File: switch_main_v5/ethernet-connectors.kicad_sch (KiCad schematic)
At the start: 9 parts, among them J2401 JST-GH-2-Horizontal, J2402 JST-GH-2-Horizontal, J2403 MSPE-J2L0-B00, J2404 MSPE-J2L0-B00, J2405 MSPE-J2L0-x00, J2406 MSPE-J2L0-x00, J2407 ARJM11D7-502-AB-EW2

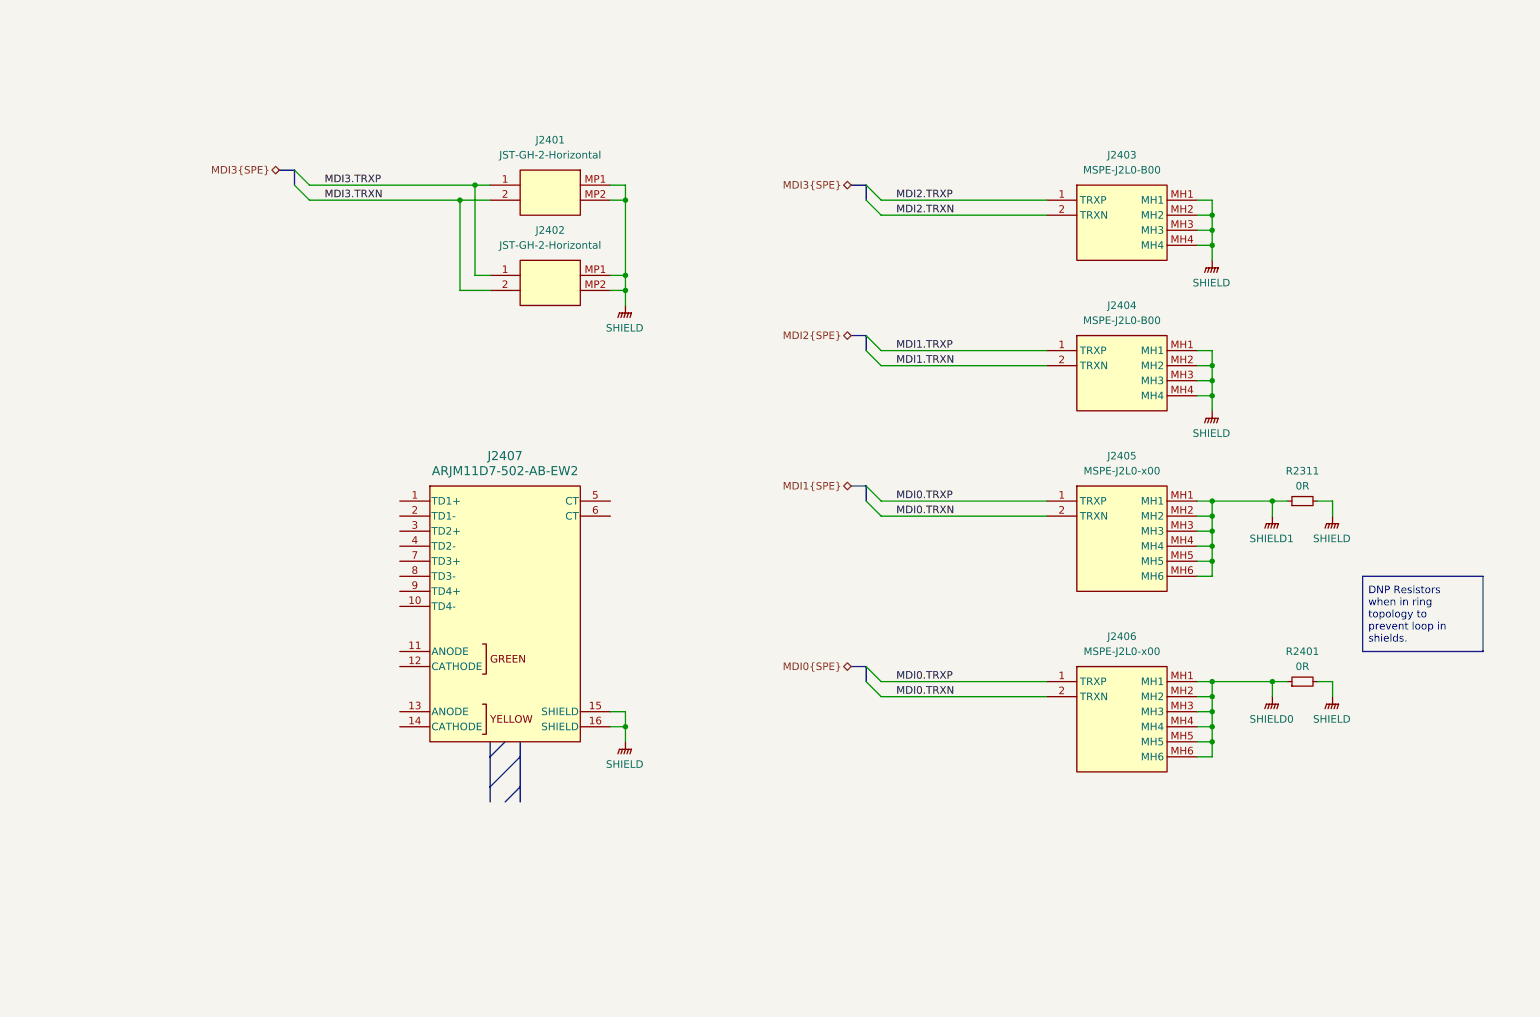
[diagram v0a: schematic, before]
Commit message: MDIO multiplexing
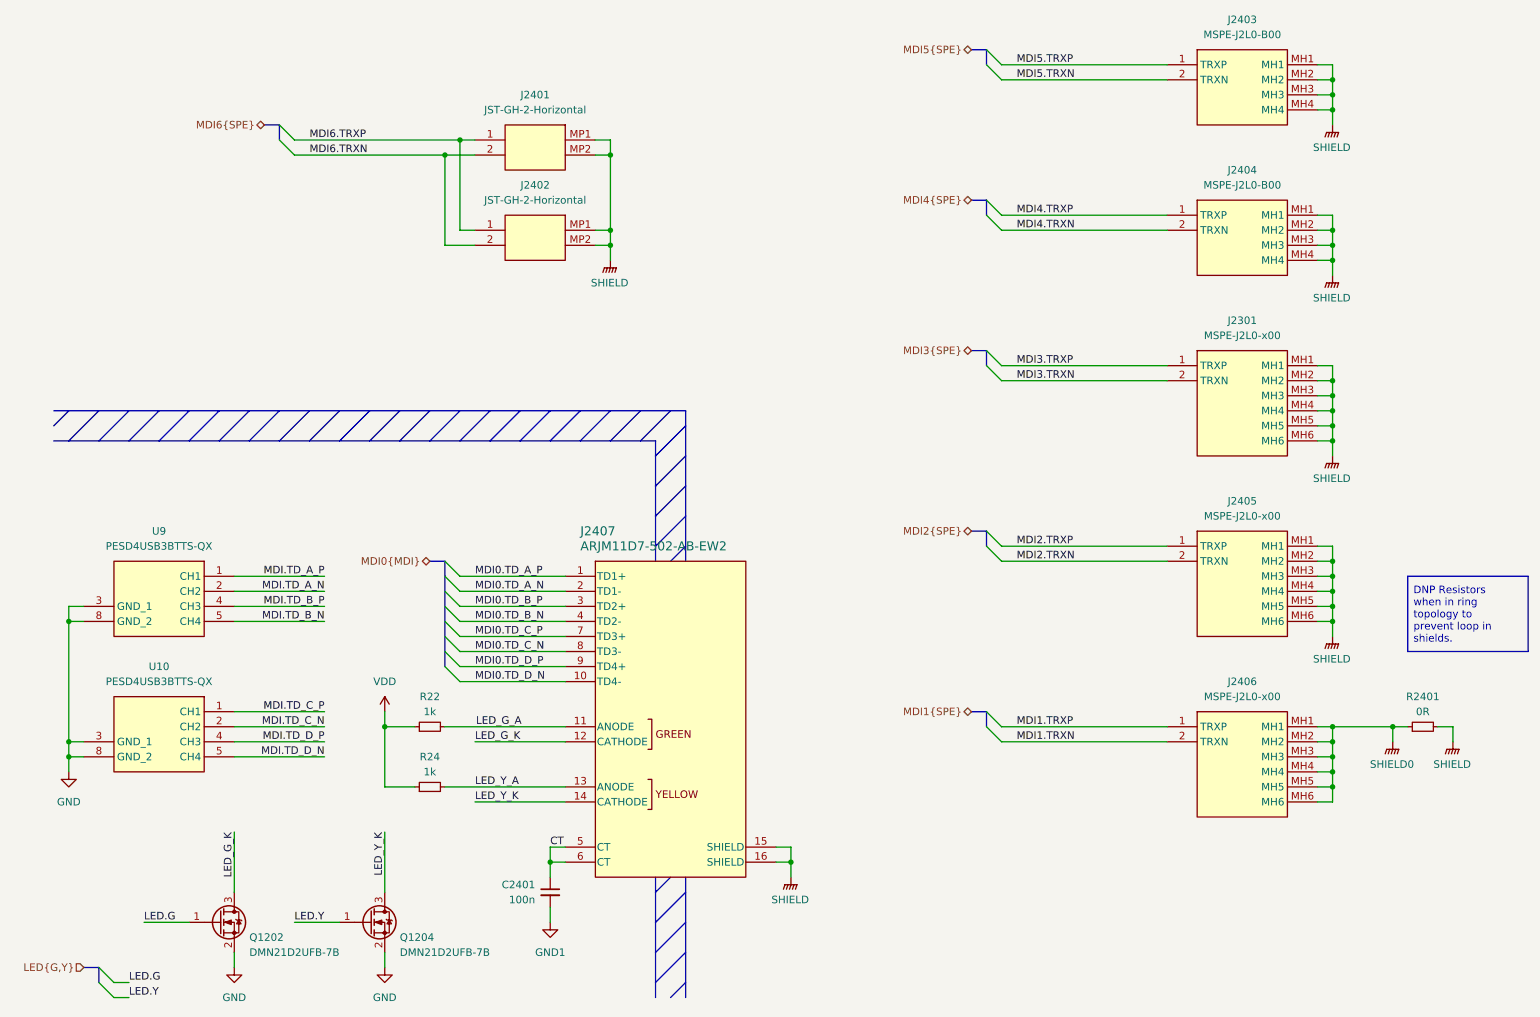
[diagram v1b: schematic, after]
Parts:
- removed R2311: 0R, Resistor_SMD:R_0402_1005Metric, symbol Device:R_Small
- added C2401: 100n, Capacitor_SMD:C_0402_1005Metric, symbol Device:C_Small
- added J2301: MSPE-J2L0-x00, project_footprints:MSPEJ2L0x00, symbol ETH-CONN:MSPE-J2L0-x00
- added Q1202, Q1204: DMN21D2UFB-7B, switch_footprints:DMN21D2UFB7B, symbol DMN21D2UFB-7B:DMN21D2UFB-7B
- added R22, R24: 1k, Resistor_SMD:R_0402_1005Metric, symbol Device:R_Small
- added U10, U9: PESD4USB3BTTS-QX, switch_footprints:PESD4USB3BTTSQX, symbol PESD4USB3BTTS-QX:PESD4USB3BTTS-QX
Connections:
- net SHIELD1 is gone; now on net SHIELD: J2405.MH1, J2405.MH2, J2405.MH3, J2405.MH4, J2405.MH5, J2405.MH6
- net MDI1.TRXN: now also J2406.2 (TRXN); no longer J2404.2 (TRXN)
- net MDI1.TRXP: now also J2406.1 (TRXP); no longer J2404.1 (TRXP)
- net MDI2.TRXN: now also J2405.2 (TRXN); no longer J2403.2 (TRXN)
- net MDI2.TRXP: now also J2405.1 (TRXP); no longer J2403.1 (TRXP)
- net MDI3.TRXN: now also J2301.2 (TRXN); no longer J2401.2, J2402.2
- net MDI3.TRXP: now also J2301.1 (TRXP); no longer J2401.1, J2402.1
- net SHIELD: now also J2301.MH1, J2301.MH2, J2301.MH3, J2301.MH4, J2301.MH5, J2301.MH6
- net MDI0.TD_A_P: now reaches J2407.1 (TD1+)
- net MDI0.TD_D_N: now reaches J2407.10 (TD4-)
- net LED_G_A: now reaches J2407.11 (ANODE)
- net LED_G_A: now also R22.2
- net LED_G_K: now reaches J2407.12 (CATHODE)
- net LED_G_K: now also Q1202.3 (D)
- net LED_Y_A: now reaches J2407.13 (ANODE)
- net LED_Y_A: now also R24.2
- net LED_Y_K: now reaches J2407.14 (CATHODE)
- net LED_Y_K: now also Q1204.3 (D)
- net MDI0.TD_A_N: now reaches J2407.2 (TD1-)
- net MDI0.TD_B_P: now reaches J2407.3 (TD2+)
- net MDI0.TD_B_N: now reaches J2407.4 (TD2-)
- net CT: now reaches J2407.5 (CT)
- net CT: now also J2407.6 (CT), C2401.1
- net MDI0.TD_C_P: now reaches J2407.7 (TD3+)
- net MDI0.TD_C_N: now reaches J2407.8 (TD3-)
- net MDI0.TD_D_P: now reaches J2407.9 (TD4+)
- removed net MDI0.TRXN: J2405.2 (TRXN), J2406.2 (TRXN)
- removed net MDI0.TRXP: J2405.1 (TRXP), J2406.1 (TRXP)
- new net GND: Q1202.2 (S), Q1204.2 (S), U10.3 (GND_1), U10.8 (GND_2), U9.3 (GND_1), U9.8 (GND_2)
- new net GND1: C2401.2
- new net LED.G: Q1202.1 (G)
- new net LED.Y: Q1204.1 (G)
- new net MDI.TD_A_N: U9.2 (CH2), U9.9 (NC)
- new net MDI.TD_A_P: U9.1 (CH1), U9.10 (NC)
- new net MDI.TD_B_N: U9.5 (CH4), U9.6 (NC)
- new net MDI.TD_B_P: U9.4 (CH3), U9.7 (NC)
- new net MDI.TD_C_N: U10.2 (CH2), U10.9 (NC)
- new net MDI.TD_C_P: U10.1 (CH1), U10.10 (NC)
- new net MDI.TD_D_N: U10.5 (CH4), U10.6 (NC)
- new net MDI.TD_D_P: U10.4 (CH3), U10.7 (NC)
- new net MDI4.TRXN: J2404.2 (TRXN)
- new net MDI4.TRXP: J2404.1 (TRXP)
- new net MDI5.TRXN: J2403.2 (TRXN)
- new net MDI5.TRXP: J2403.1 (TRXP)
- new net MDI6.TRXN: J2401.2, J2402.2
- new net MDI6.TRXP: J2401.1, J2402.1
- new net VDD: R22.1, R24.1
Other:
- moved on the sheet: J2401, J2402, J2403, J2404, J2405, J2406, J2407, R2401

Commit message: Updated 1v0_buck_converter feedback resistors
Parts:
- renumbered J2407 to J2403, J2403 to J2404, J2404 to J2405, J2301 to J2406, J2405 to J2407, J2406 to J2408, Q1202 to Q2401, Q1204 to Q2402, R22 to R2401, R24 to R2402, R2401 to R2403, U9 to U2401, U10 to U2402

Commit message: Changed main 3V3 regulator to 3A, added switch 2 crystal & other changes
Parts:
- Q2401, Q2402: footprint switch_footprints:DMN21D2UFB7B -> project_footprints:DMN21D2UFB7B; symbol DMN21D2UFB-7B:DMN21D2UFB-7B -> MOSFET:DMN21D2UFB-7B
- U2401, U2402: footprint switch_footprints:PESD4USB3BTTSQX -> project_footprints:PESD4USB3BTTSQX; symbol PESD4USB3BTTS-QX:PESD4USB3BTTS-QX -> TVS:PESD4USB3BTTS-QX
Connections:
- net GND is gone; now on net GND1: Q2401.2 (S), Q2402.2 (S), U2401.3 (GND_1), U2401.8 (GND_2), U2402.3 (GND_1), U2402.8 (GND_2)
- net MDI.TD_A_N is gone; now on net MDI0.TD_A_N: U2401.2 (CH2), U2401.9 (NC)
- net MDI.TD_A_P is gone; now on net MDI0.TD_A_P: U2401.1 (CH1), U2401.10 (NC)
- net MDI.TD_B_N is gone; now on net MDI0.TD_B_N: U2401.5 (CH4), U2401.6 (NC)
- net MDI.TD_B_P is gone; now on net MDI0.TD_B_P: U2401.4 (CH3), U2401.7 (NC)
- net MDI.TD_C_N is gone; now on net MDI0.TD_C_N: U2402.2 (CH2), U2402.9 (NC)
- net MDI.TD_C_P is gone; now on net MDI0.TD_C_P: U2402.1 (CH1), U2402.10 (NC)
- net MDI.TD_D_N is gone; now on net MDI0.TD_D_N: U2402.5 (CH4), U2402.6 (NC)
- net MDI.TD_D_P is gone; now on net MDI0.TD_D_P: U2402.4 (CH3), U2402.7 (NC)
- net VDD renamed +3V3

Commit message: Placed 1000BASE-T PHY decoupling capacitors
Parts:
- U2401, U2402: now not fitted; now left out of the parts list
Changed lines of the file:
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@@
 		(members "TRXP" "TRXN")
 	)
+	(text_box "The 1000BASE-T PHY has 8kV of ESD protection and is galvanically isolated so more TVS diodes are likely unecessary"
+		(exclude_from_sim no)
+		(at 48.26 96.52 0)
+		(size 27.94 12.7)
+		(margins 0.9525 0.9525 0.9525 0.9525)
+		(stroke
+			(width 0)
+			(type solid)
+		)
+		(fill
+			(type none)
+		)
+		(effects
+			(font
+				(size 1.27 1.27)
+			)
+		)
+	)
 	(text_box "DNP Resistors when in ring topology to prevent loop in shields."
 		(exclude_from_sim no)
@@
 		(unit 1)
 		(exclude_from_sim no)
-		(in_bom yes)
-		(on_board yes)
-		(dnp no)
+		(in_bom no)
+		(on_board no)
+		(dnp yes)
 		(fields_autoplaced yes)
 		(property "Reference" "U2402"
@@
 		(unit 1)
 		(exclude_from_sim no)
-		(in_bom yes)
-		(on_board yes)
-		(dnp no)
+		(in_bom no)
+		(on_board no)
+		(dnp yes)
 		(fields_autoplaced yes)
 		(property "Reference" "U2401"

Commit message: Tidied schematic and PCB
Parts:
- renumbered C2401 to C3601, J2404 to J3601, J2401 to J3602, J2405 to J3603, J2402 to J3604, J2406 to J3605, J2407 to J3606, J2403 to J3607, J2408 to J3608, Q2401 to Q3601, Q2402 to Q3602, R2401 to R3601, R2403 to R3602, R2402 to R3603, U2401 to U3601, U2402 to U3602
